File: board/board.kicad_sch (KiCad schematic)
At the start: 61 parts, among them J1 Conn_01x25_Socket, J2 Conn_01x25_Socket, J5 PJ-320B, J6 Screw_Terminal_01x02, J7 Screw_Terminal_01x02, J8 Screw_Terminal_01x02

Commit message: attempt at tracing v2
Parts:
- removed C1, C13, C2, C3, C4: 0.22uF_0603_25V, 4ms_Capacitor:C_0603, symbol 4ms_Capacitor:0.22uF_0603_25V
- added C13, C14, C18, C21, C4, C8, C9: 22uF_0603_16V, 4ms_Capacitor:C_0805, symbol 4ms_Capacitor:22uF_0603_16V
- renumbered C5 to C1, C11 to C10, C14 to C11, C16 to C15, C15 to C16, C6 to C2, C18 to C20, C20 to C22, C21 to C24, C22 to C25, C7 to C3, C8 to C5, C9 to C6, C10 to C7, J4 to J1, J3 to J2, J1 to J3, J2 to J4, R11 to R1, R8 to R10, R6 to R11, R13 to R12, R7 to R13, R15 to R14, R10 to R15, R12 to R2, R1 to R3, R2 to R4, R3 to R5, R14 to R6, R4 to R7, R9 to R8, R5 to R9, U4 to U1, U12 to U11, U14 to U12, U1 to U13, U13 to U14, U5 to U4, U6 to U5, U7 to U6, U11 to U7
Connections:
- net PC1 is gone; now on net NOISE_CLK_SEL: J4.16 (Pin_16)
- net CH1_TOVOL: now also U5.6 (D2), C8.2; no longer U5.10 (D1), U8.16 (VinL)
- net CH2_TOVOL: now also U5.10 (D1), C4.2; no longer U5.6 (D2), U8.9 (VinR)
- net CH3_TOVOL: now also C13.2; no longer U9.16 (VinL)
- net CH4_TOVOL: now also C9.2; no longer U9.9 (VinR)
- net DAC_tovol1: now also C18.2; no longer U12.9 (VinR)
- net DAC_tovol2: now also C21.2; no longer U12.16 (VinL)
- net DDS1_out: now also U5.7 (S2B); no longer U5.2 (S1A)
- net DDS2_out: now also U5.9 (S1B); no longer U5.4 (S2A)
- net NOISE_CLK_SEL: no longer J3.19 (Pin_19)
- net NOISE_TOVOL: now also C14.2; no longer U10.9 (VinR)
- net PWM1: now also U5.4 (S2A); no longer U5.9 (S1B)
- net PWM2: now also U5.2 (S1A); no longer U5.7 (S2B)
- new net: C9.1, U9.9 (VinR)
- new net: C4.1, U8.9 (VinR)
- new net: C8.1, U8.16 (VinL)
- new net: C21.1, U12.16 (VinL)
- new net: C13.1, U9.16 (VinL)
- new net: C18.1, U12.9 (VinR)
- new net: C14.1, U10.9 (VinR)
- new net PB2: J3.19 (Pin_19)
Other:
- moved on the sheet: C10, C11, C12, C15, C16, C17, C19, C20, C22, C24, C25, R1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

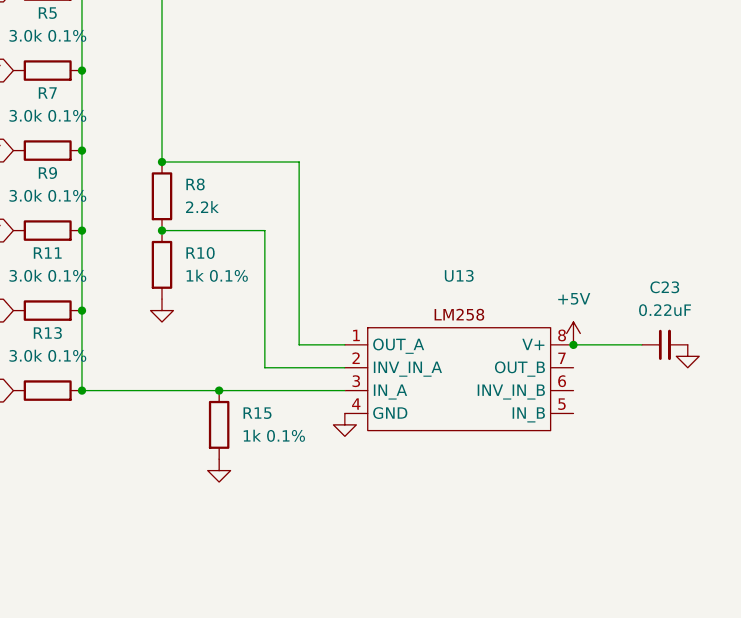
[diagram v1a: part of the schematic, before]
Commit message: new opamp, timers init
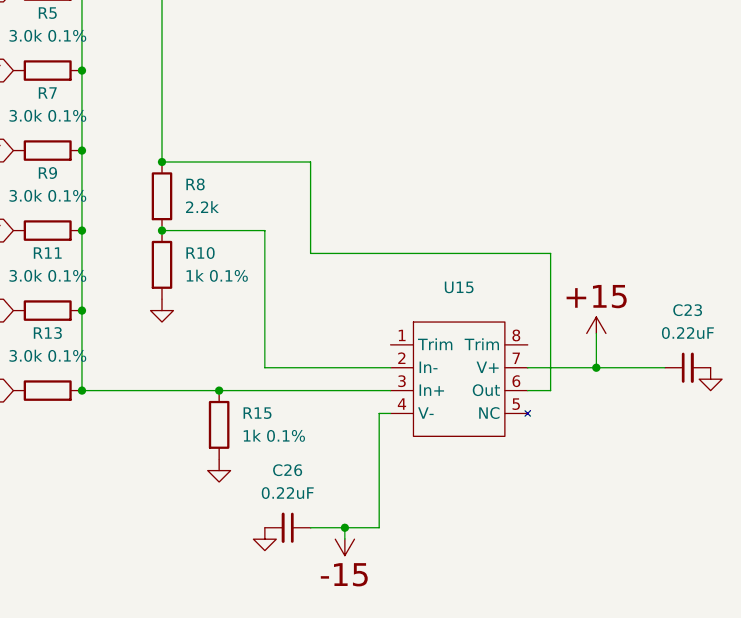
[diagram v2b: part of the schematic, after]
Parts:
- removed U13: ~, Package_SO:SOIC-8_3.9x4.9mm_P1.27mm, symbol project:LM258
- added C26: 0.22uF_0603_25V, 4ms_Capacitor:C_0603, symbol 4ms_Capacitor:0.22uF_0603_25V
- added U15: ~, Package_SO:SOP-8_3.76x4.96mm_P1.27mm, symbol project:OPA227
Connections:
- net +5V: no longer C23.1
- net GND: now also C26.2
- net P,+15: now also C23.1, U15.7 (V+)
- net P,-15: now also C26.1, U15.4 (V-)
- net at R11.2, R13.2, R15.1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: now also U15.3 (In+)
- net at J5.1, J5.2, R8.1: now also U15.6 (Out)
- net at R10.1, R8.2: now also U15.2 (In-)
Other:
- moved on the sheet: C23

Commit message: more board rework, UART & SPI init
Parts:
- removed H1: MountingHole, MountingHole:MountingHole_3.2mm_M3, symbol Mechanical:MountingHole
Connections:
- net PB10 is gone; now on net CS_AD9833_3: J3.18 (Pin_18)
- net PB11 is gone; now on net CS_AD9833_4: J3.17 (Pin_17)
- net PB12/adc4_in3 is gone; now on net ZCEN_2: J3.16 (Pin_16)
- net PB14/adc4_in4 is gone; now on net ZCEN_DAC: J3.14 (Pin_14)
- net PB2 is gone; now on net ZCEN_1: J3.19 (Pin_19)
- net PC4/adc2_in5 is gone; now on net CS_AD9833_2: J3.23 (Pin_23)
- net PC5/adc2_in11 is gone; now on net CS_AD9833_1: J3.22 (Pin_22)
- net ATTEN_CS: now also J3.12 (Pin_12); no longer J4.21 (Pin_21)
- net CS_AD9833_1: no longer J4.22 (Pin_22)
- net CS_AD9833_2: no longer J3.7 (Pin_7)
- net CS_AD9833_3: no longer J3.6 (Pin_6)
- net CS_AD9833_4: no longer J4.5 (Pin_5)
- net MUX_SEL_1: now also J4.21 (Pin_21); no longer J4.18 (Pin_18)
- net MUX_SEL_2: now also J4.22 (Pin_22); no longer J4.19 (Pin_19)
- net MUX_SEL_3: now also J4.19 (Pin_19); no longer J4.14 (Pin_14)
- net MUX_SEL_4: now also J4.18 (Pin_18); no longer J4.15 (Pin_15)
- net NOISE_CLK_SEL: now also J4.14 (Pin_14); no longer J4.16 (Pin_16)
- net NOISE_CS: now also J4.15 (Pin_15); no longer J4.4 (Pin_4)
- net ZCEN_1: no longer J3.12 (Pin_12)
- net ZCEN_2: no longer J3.11 (Pin_11)
- net ZCEN_DAC: no longer J3.9 (Pin_9)
- new net PA10: J3.6 (Pin_6)
- new net PA15: J4.4 (Pin_4)
- new net PA9: J3.7 (Pin_7)
- new net PC1: J4.16 (Pin_16)
- new net PC12: J4.5 (Pin_5)
- new net PC7: J3.11 (Pin_11)
- new net PC9: J3.9 (Pin_9)

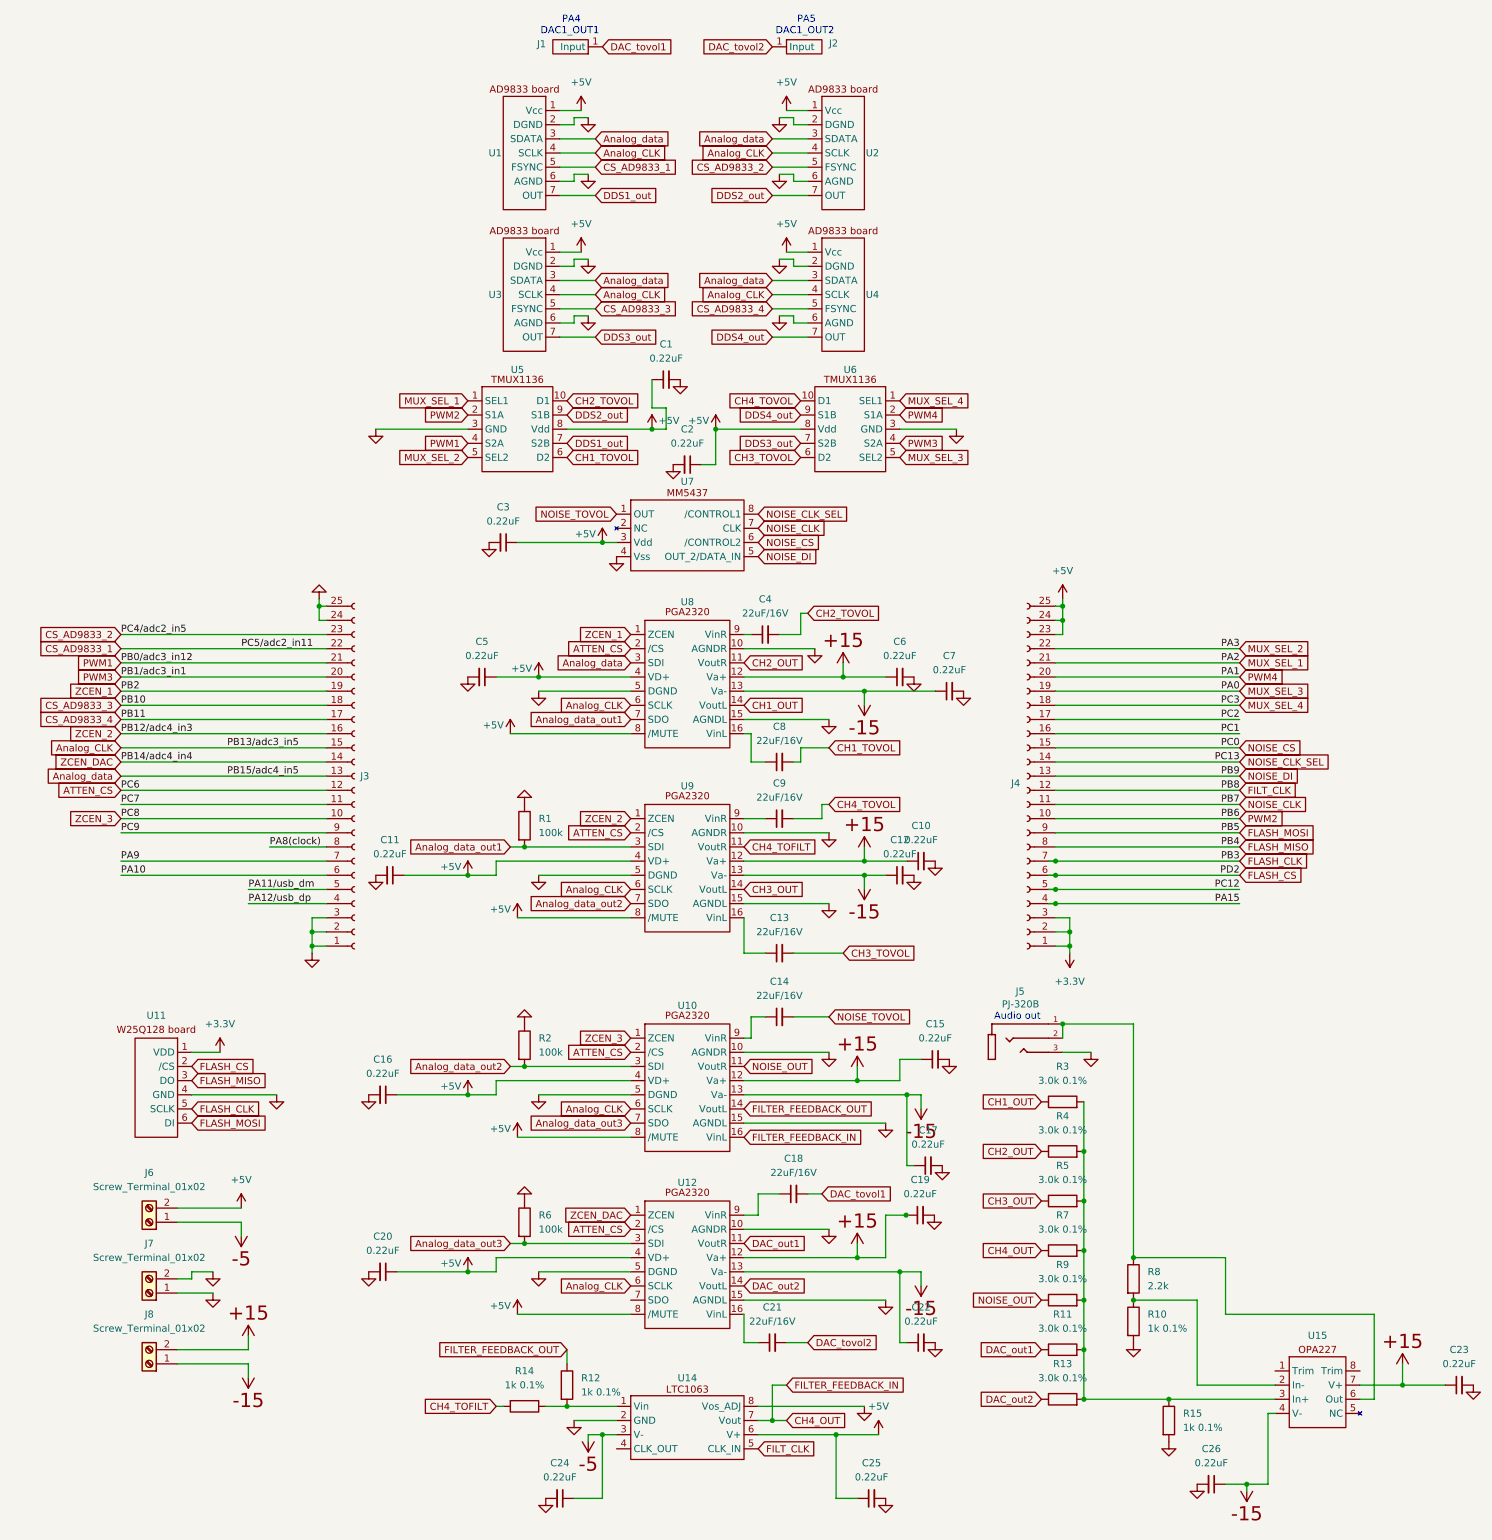
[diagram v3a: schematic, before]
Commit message: added DMA init
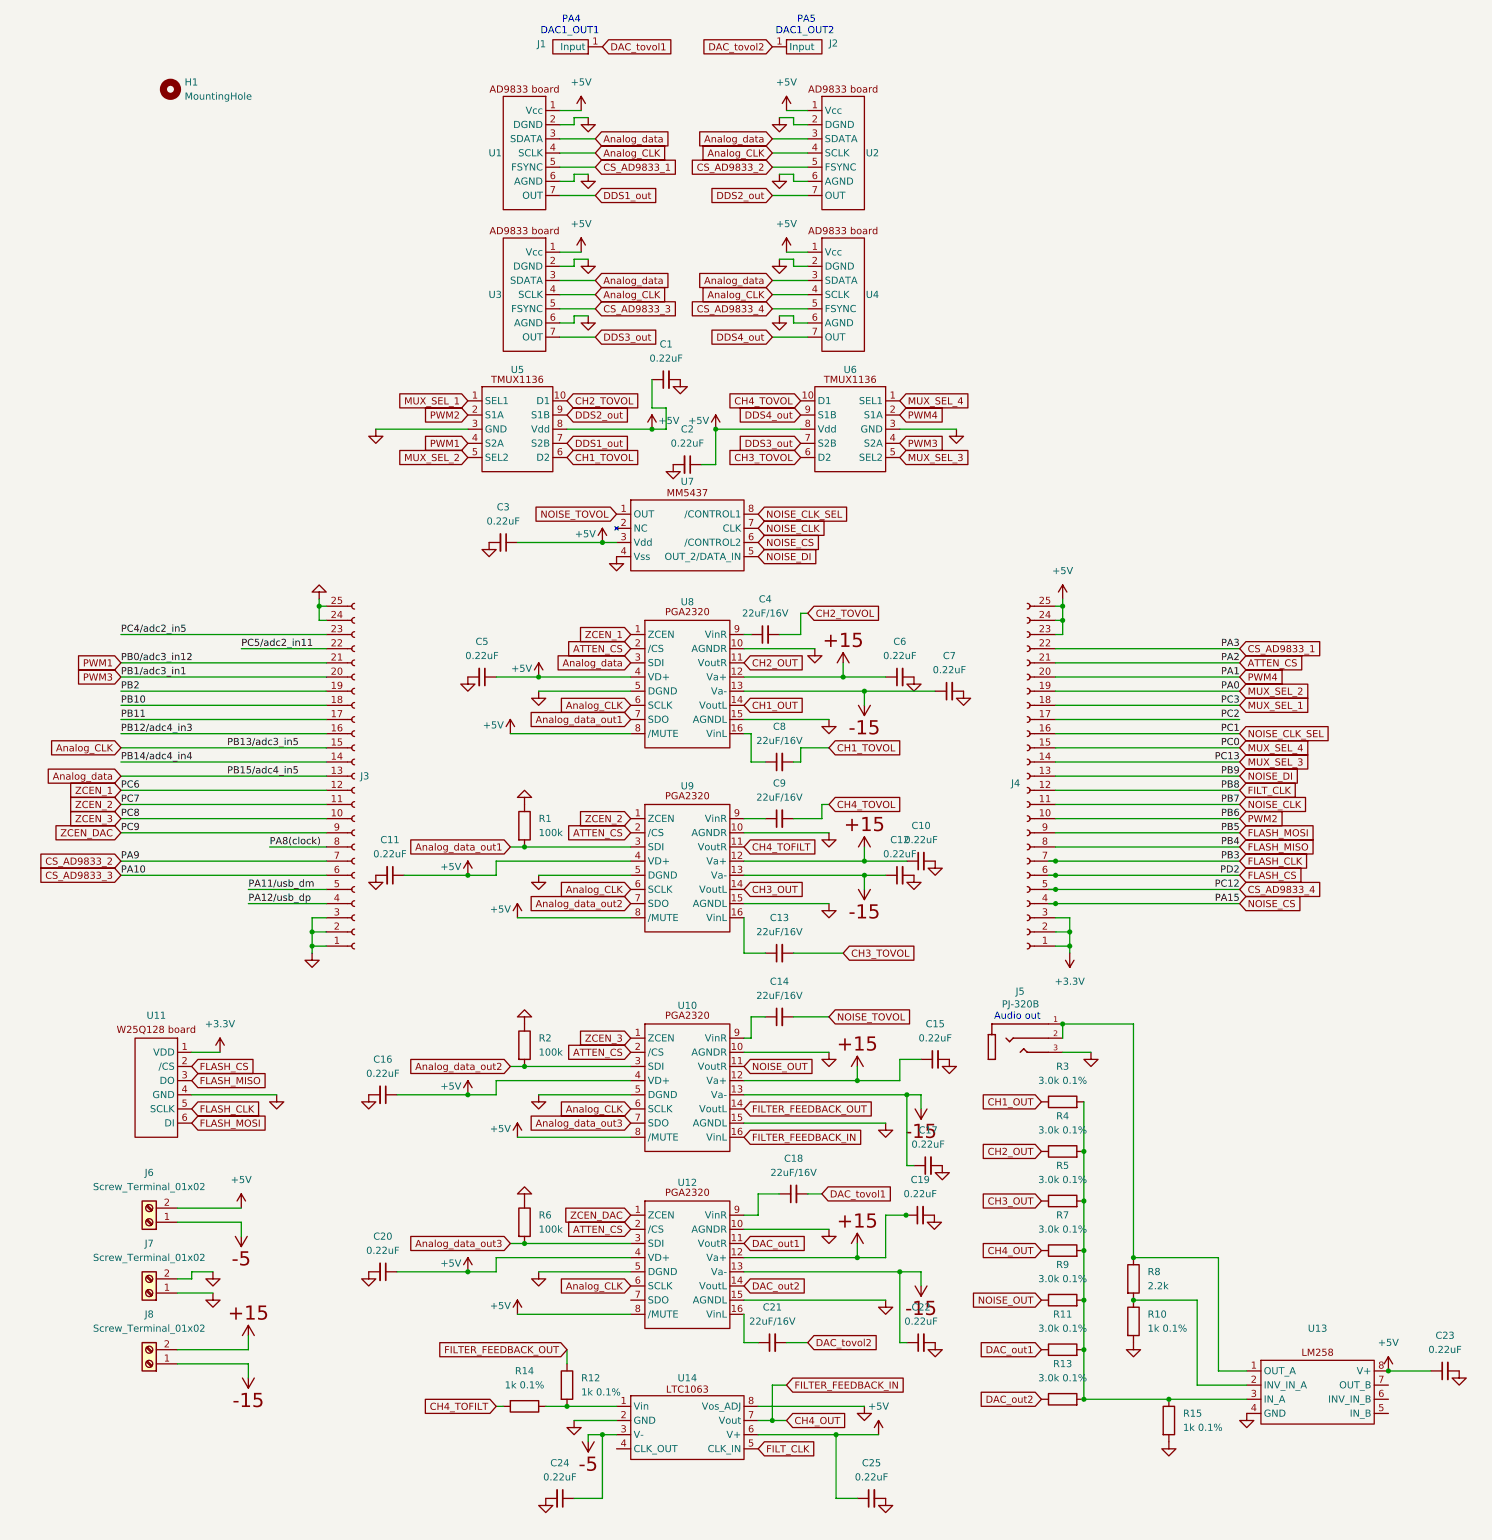
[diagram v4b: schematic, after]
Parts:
- removed C26: 0.22uF_0603_25V, 4ms_Capacitor:C_0603, symbol 4ms_Capacitor:0.22uF_0603_25V
- removed U15: ~, Package_SO:SOP-8_3.76x4.96mm_P1.27mm, symbol project:OPA227
- added H1: MountingHole, MountingHole:MountingHole_3.2mm_M3, symbol Mechanical:MountingHole
- added U13: ~, Package_SO:SOIC-8_3.9x4.9mm_P1.27mm, symbol project:LM258
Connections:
- net PA10 is gone; now on net CS_AD9833_3: J3.6 (Pin_6)
- net PA15 is gone; now on net NOISE_CS: J4.4 (Pin_4)
- net PA9 is gone; now on net CS_AD9833_2: J3.7 (Pin_7)
- net PC1 is gone; now on net NOISE_CLK_SEL: J4.16 (Pin_16)
- net PC12 is gone; now on net CS_AD9833_4: J4.5 (Pin_5)
- net PC7 is gone; now on net ZCEN_2: J3.11 (Pin_11)
- net PC9 is gone; now on net ZCEN_DAC: J3.9 (Pin_9)
- net +5V: now also C23.1, U13.8 (V+)
- net ATTEN_CS: now also J4.21 (Pin_21); no longer J3.12 (Pin_12)
- net CS_AD9833_1: now also J4.22 (Pin_22); no longer J3.22 (Pin_22)
- net CS_AD9833_2: no longer J3.23 (Pin_23)
- net CS_AD9833_3: no longer J3.18 (Pin_18)
- net CS_AD9833_4: no longer J3.17 (Pin_17)
- net GND: now also U13.4 (GND)
- net MUX_SEL_1: now also J4.18 (Pin_18); no longer J4.21 (Pin_21)
- net MUX_SEL_2: now also J4.19 (Pin_19); no longer J4.22 (Pin_22)
- net MUX_SEL_3: now also J4.14 (Pin_14); no longer J4.19 (Pin_19)
- net MUX_SEL_4: now also J4.15 (Pin_15); no longer J4.18 (Pin_18)
- net NOISE_CLK_SEL: no longer J4.14 (Pin_14)
- net NOISE_CS: no longer J4.15 (Pin_15)
- net P,+15: no longer C23.1
- net ZCEN_1: now also J3.12 (Pin_12); no longer J3.19 (Pin_19)
- net ZCEN_2: no longer J3.16 (Pin_16)
- net ZCEN_DAC: no longer J3.14 (Pin_14)
- net at R10.1, R8.2: now also U13.2 (INV_IN_A)
- net at R11.2, R13.2, R15.1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: now also U13.3 (IN_A)
- net at J5.1, J5.2, R8.1: now also U13.1 (OUT_A)
- new net PB10: J3.18 (Pin_18)
- new net PB11: J3.17 (Pin_17)
- new net PB12/adc4_in3: J3.16 (Pin_16)
- new net PB14/adc4_in4: J3.14 (Pin_14)
- new net PB2: J3.19 (Pin_19)
- new net PC4/adc2_in5: J3.23 (Pin_23)
- new net PC5/adc2_in11: J3.22 (Pin_22)
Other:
- moved on the sheet: C23
